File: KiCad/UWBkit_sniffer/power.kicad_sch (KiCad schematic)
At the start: 0 parts

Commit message: Added components to schematic
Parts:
- added C10, C9: 10u, Capacitor_SMD:C_0603_1608Metric, symbol Device:C_Small
- added C8: 100n, Capacitor_SMD:C_0603_1608Metric, symbol Device:C_Small
- added D4: R, LED_SMD:LED_0603_1608Metric, symbol Device:LED_Small
- added L3: 2.2u, Inductor_SMD:L_0805_2012Metric, symbol Device:L_Small
- added R8: 3k3, Resistor_SMD:R_0603_1608Metric, symbol Device:R_Small
- added TP8: TestPoint_Small, TestPoint:TestPoint_Pad_D1.0mm, symbol Connector:TestPoint_Small
- added U4: XC9285B33CMR-G, Package_TO_SOT_SMD:SOT-23-5, symbol DCDC_Converter_Custom:XC9285B33CMR-G
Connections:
- new net: L3.1, U4.5 (Lx)
- new net: D4.1 (K), R8.1
- new net +3V3: C10.1, D4.2 (A), L3.2, TP8.1, U4.4 (VOUT)
- new net +5V: C8.1, C9.1, U4.1 (VIN), U4.3 (EN)
- new net GND: C10.2, C8.2, C9.2, R8.2, U4.2 (GND)
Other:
- note added: "Power LED"
- note added: "Unnecessary when using the USB peripheral directly"

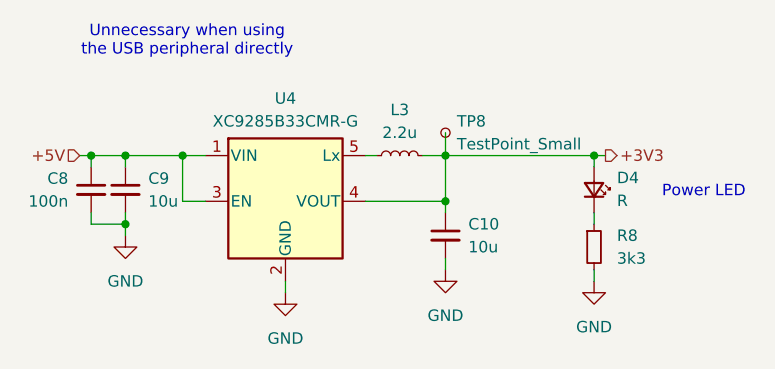
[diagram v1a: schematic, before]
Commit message: United 5V rails, modified layout of connectors
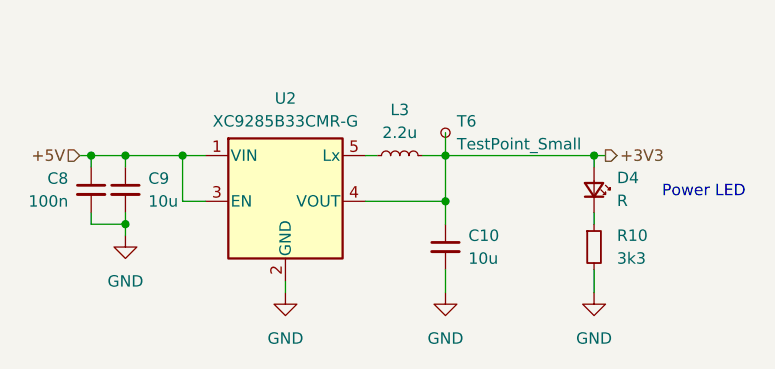
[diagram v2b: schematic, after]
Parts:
- renumbered R8 to R10, TP8 to T6, U4 to U2
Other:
- note removed: "Unnecessary when using the USB peripheral directly"
- moved on the sheet: C10
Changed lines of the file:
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@@
-		)
-	)
-	(text "Unnecessary when using \nthe USB peripheral directly"
-		(exclude_from_sim no)
-		(at 121.158 81.28 0)
-		(effects
-			(font
-				(size 1.27 1.27)
-			)
 		)
 	)
@@
 	(wire
 		(pts
-			(xy 149.86 99.06) (xy 149.86 100.33)
-		)
-		(stroke
-			(width 0)
-			(type default)
-		)
-	)
-	(wire
-		(pts
-			(xy 166.37 106.68) (xy 166.37 107.95)
+			(xy 149.86 99.06) (xy 149.86 101.6)
+		)
+		(stroke
+			(width 0)
+			(type default)
+		)
+	)
+	(wire
+		(pts
+			(xy 166.37 106.68) (xy 166.37 109.22)
 		)
 		(stroke
@@
 	(wire
 		(pts
-			(xy 149.86 105.41) (xy 149.86 106.68)
+			(xy 149.86 106.68) (xy 149.86 109.22)
 		)
 		(stroke
@@
 		(dnp no)
 		(fields_autoplaced yes)
-		(property "Reference" "#PWR034"
+		(property "Reference" "#PWR048"
 			(at 132.08 115.57 0)
 			(effects
@@
 			(project "UWBkit_sniffer"
 				(path "/7666dc1a-7b28-48ea-a5e3-eea89f700cea/10e613d1-a26e-4277-8fad-c08e21526a22"
-					(reference "#PWR034")
+					(reference "#PWR048")
 					(unit 1)
 				)
@@
 	(symbol
 		(lib_id "Device:C_Small")
-		(at 149.86 102.87 0)
+		(at 149.86 104.14 0)
 		(unit 1)
 		(exclude_from_sim no)
@@
 		(dnp no)
 		(property "Reference" "C10"
-			(at 152.4 101.6062 0)
+			(at 152.4 102.8762 0)
 			(effects
 				(font
@@
 		)
 		(property "Value" "10u"
-			(at 152.4 104.1462 0)
+			(at 152.4 105.4162 0)
 			(effects
 				(font
@@
 		)
 		(property "Footprint" "Capacitor_SMD:C_0603_1608Metric"
-			(at 149.86 102.87 0)
+			(at 149.86 104.14 0)
 			(effects
 				(font
@@
 		)
 		(property "Datasheet" "~"
-			(at 149.86 102.87 0)
+			(at 149.86 104.14 0)
 			(effects
 				(font
@@
 		)
 		(property "Description" "Unpolarized capacitor, small symbol"
-			(at 149.86 102.87 0)
+			(at 149.86 104.14 0)
 			(effects
 				(font
@@
 		(on_board yes)
 		(dnp no)
-		(property "Reference" "TP8"
+		(property "Reference" "T6"
 			(at 151.13 90.1699 0)
 			(effects
@@
 			(project "UWBkit_sniffer"
 				(path "/7666dc1a-7b28-48ea-a5e3-eea89f700cea/10e613d1-a26e-4277-8fad-c08e21526a22"
-					(reference "TP8")
+					(reference "T6")
 					(unit 1)
 				)
@@
 	(symbol
 		(lib_id "power:GND")
-		(at 149.86 106.68 0)
+		(at 149.86 109.22 0)
 		(unit 1)
 		(exclude_from_sim no)
@@
 		(dnp no)
 		(fields_autoplaced yes)
-		(property "Reference" "#PWR032"
-			(at 149.86 113.03 0)
+		(property "Reference" "#PWR049"
+			(at 149.86 115.57 0)
 			(effects
 				(font
@@
 		)
 		(property "Value" "GND"
-			(at 149.86 111.76 0)
+			(at 149.86 114.3 0)
 			(effects
 				(font
@@
 		)
 		(property "Footprint" ""
-			(at 149.86 106.68 0)
+			(at 149.86 109.22 0)
 			(effects
 				(font
@@
 		)
 		(property "Datasheet" ""
-			(at 149.86 106.68 0)
+			(at 149.86 109.22 0)
 			(effects
 				(font
@@
 		)
 		(property "Description" "Power symbol creates a global label with name \"GND\" , ground"
-			(at 149.86 106.68 0)
+			(at 149.86 109.22 0)
 			(effects
 				(font
@@
 			(project "UWBkit_sniffer"
 				(path "/7666dc1a-7b28-48ea-a5e3-eea89f700cea/10e613d1-a26e-4277-8fad-c08e21526a22"
-					(reference "#PWR032")
+					(reference "#PWR049")
 					(unit 1)
 				)
@@
 	(symbol
 		(lib_id "power:GND")
-		(at 166.37 107.95 0)
+		(at 166.37 109.22 0)
 		(unit 1)
 		(exclude_from_sim no)
@@
 		(dnp no)
 		(fields_autoplaced yes)
-		(property "Reference" "#PWR033"
+		(property "Reference" "#PWR050"
+			(at 166.37 115.57 0)
+			(effects
+				(font
+					(size 1.27 1.27)
+				)
+				(hide yes)
+			)
+		)
+		(property "Value" "GND"
 			(at 166.37 114.3 0)
 			(effects
@@
 					(size 1.27 1.27)
 				)
-				(hide yes)
-			)
-		)
-		(property "Value" "GND"
-			(at 166.37 113.03 0)
-			(effects
-				(font
-					(size 1.27 1.27)
-				)
 			)
 		)
 		(property "Footprint" ""
-			(at 166.37 107.95 0)
+			(at 166.37 109.22 0)
 			(effects
 				(font
@@
 		)
 		(property "Datasheet" ""
-			(at 166.37 107.95 0)
+			(at 166.37 109.22 0)
 			(effects
 				(font
@@
 		)
 		(property "Description" "Power symbol creates a global label with name \"GND\" , ground"
-			(at 166.37 107.95 0)
+			(at 166.37 109.22 0)
 			(effects
 				(font
@@
 			(project "UWBkit_sniffer"
 				(path "/7666dc1a-7b28-48ea-a5e3-eea89f700cea/10e613d1-a26e-4277-8fad-c08e21526a22"
-					(reference "#PWR033")
+					(reference "#PWR050")
 					(unit 1)
 				)
@@
 		(dnp no)
 		(fields_autoplaced yes)
-		(property "Reference" "U4"
+		(property "Reference" "U2"
 			(at 132.08 87.63 0)
 			(effects
@@
 			(project "UWBkit_sniffer"
 				(path "/7666dc1a-7b28-48ea-a5e3-eea89f700cea/10e613d1-a26e-4277-8fad-c08e21526a22"
-					(reference "U4")
+					(reference "U2")
 					(unit 1)
 				)
@@
 		(dnp no)
 		(fields_autoplaced yes)
-		(property "Reference" "R8"
+		(property "Reference" "R10"
 			(at 168.91 102.8699 0)
 			(effects
@@
 			(project "UWBkit_sniffer"
 				(path "/7666dc1a-7b28-48ea-a5e3-eea89f700cea/10e613d1-a26e-4277-8fad-c08e21526a22"
-					(reference "R8")
+					(reference "R10")
 					(unit 1)
 				)
@@
 		(dnp no)
 		(fields_autoplaced yes)
-		(property "Reference" "#PWR030"
+		(property "Reference" "#PWR047"
 			(at 114.3 109.22 0)
 			(effects
@@
 			(project "UWBkit_sniffer"
 				(path "/7666dc1a-7b28-48ea-a5e3-eea89f700cea/10e613d1-a26e-4277-8fad-c08e21526a22"
-					(reference "#PWR030")
+					(reference "#PWR047")
 					(unit 1)
 				)

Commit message: Removed UWA.01, added CTS/RTS connections
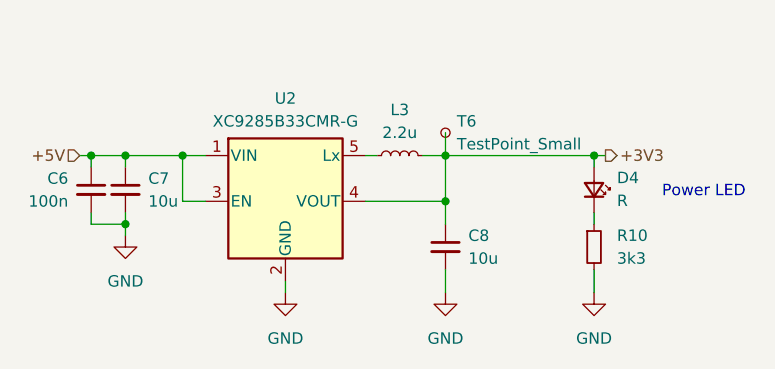
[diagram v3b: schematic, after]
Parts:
- renumbered C8 to C6, C9 to C7, C10 to C8
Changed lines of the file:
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@@
 		(dnp no)
 		(fields_autoplaced yes)
-		(property "Reference" "#PWR048"
+		(property "Reference" "#PWR047"
 			(at 132.08 115.57 0)
 			(effects
@@
 			(project "UWBkit_sniffer"
 				(path "/7666dc1a-7b28-48ea-a5e3-eea89f700cea/10e613d1-a26e-4277-8fad-c08e21526a22"
-					(reference "#PWR048")
+					(reference "#PWR047")
 					(unit 1)
 				)
@@
 		(on_board yes)
 		(dnp no)
-		(property "Reference" "C10"
+		(property "Reference" "C8"
 			(at 152.4 102.8762 0)
 			(effects
@@
 			(project "UWBkit_sniffer"
 				(path "/7666dc1a-7b28-48ea-a5e3-eea89f700cea/10e613d1-a26e-4277-8fad-c08e21526a22"
-					(reference "C10")
+					(reference "C8")
 					(unit 1)
 				)
@@
 		(on_board yes)
 		(dnp no)
-		(property "Reference" "C9"
+		(property "Reference" "C7"
 			(at 116.84 96.5262 0)
 			(effects
@@
 			(project "UWBkit_sniffer"
 				(path "/7666dc1a-7b28-48ea-a5e3-eea89f700cea/10e613d1-a26e-4277-8fad-c08e21526a22"
-					(reference "C9")
+					(reference "C7")
 					(unit 1)
 				)
@@
 		(on_board yes)
 		(dnp no)
-		(property "Reference" "C8"
+		(property "Reference" "C6"
 			(at 107.95 96.5262 0)
 			(effects
@@
 			(project "UWBkit_sniffer"
 				(path "/7666dc1a-7b28-48ea-a5e3-eea89f700cea/10e613d1-a26e-4277-8fad-c08e21526a22"
-					(reference "C8")
+					(reference "C6")
 					(unit 1)
 				)
@@
 		(dnp no)
 		(fields_autoplaced yes)
-		(property "Reference" "#PWR049"
+		(property "Reference" "#PWR048"
 			(at 149.86 115.57 0)
 			(effects
@@
 			(project "UWBkit_sniffer"
 				(path "/7666dc1a-7b28-48ea-a5e3-eea89f700cea/10e613d1-a26e-4277-8fad-c08e21526a22"
-					(reference "#PWR049")
+					(reference "#PWR048")
 					(unit 1)
 				)
@@
 		(dnp no)
 		(fields_autoplaced yes)
-		(property "Reference" "#PWR050"
+		(property "Reference" "#PWR049"
 			(at 166.37 115.57 0)
 			(effects
@@
 			(project "UWBkit_sniffer"
 				(path "/7666dc1a-7b28-48ea-a5e3-eea89f700cea/10e613d1-a26e-4277-8fad-c08e21526a22"
-					(reference "#PWR050")
+					(reference "#PWR049")
 					(unit 1)
 				)
@@
 		(dnp no)
 		(fields_autoplaced yes)
-		(property "Reference" "#PWR047"
+		(property "Reference" "#PWR046"
 			(at 114.3 109.22 0)
 			(effects
@@
 			(project "UWBkit_sniffer"
 				(path "/7666dc1a-7b28-48ea-a5e3-eea89f700cea/10e613d1-a26e-4277-8fad-c08e21526a22"
-					(reference "#PWR047")
-					(unit 1)
-				)
+					(reference "#PWR046")
+					(unit 1)
+				)

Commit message: Improved placement of ICs and ports and the board is now smaller
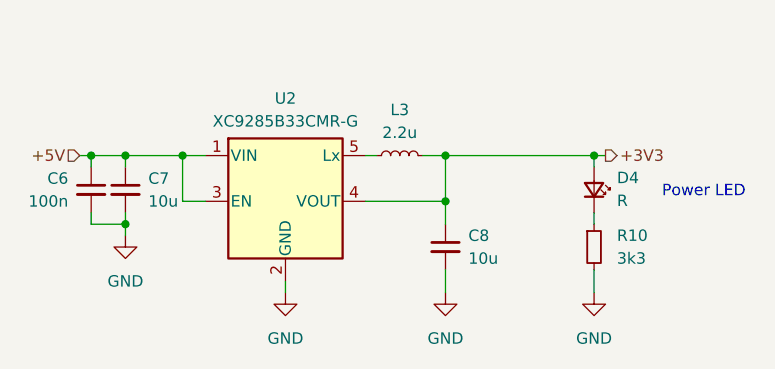
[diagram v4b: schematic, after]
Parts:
- removed T6: TestPoint_Small, TestPoint:TestPoint_Pad_D1.0mm, symbol Connector:TestPoint_Small
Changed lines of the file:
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@@
-	(wire
-		(pts
-			(xy 149.86 91.44) (xy 149.86 93.98)
-		)
-		(stroke
-			(width 0)
-			(type default)
-		)
-	)
 	(wire
 		(pts
@@
 					(unit 1)
 				)
-			)
-		)
-	)
-	(symbol
-		(lib_id "Connector:TestPoint_Small")
-		(at 149.86 91.44 0)
-		(unit 1)
-		(exclude_from_sim no)
-		(in_bom no)
-		(on_board yes)
-		(dnp no)
-		(property "Reference" "T6"
-			(at 151.13 90.1699 0)
-			(effects
-				(font
-					(size 1.27 1.27)
-				)
-				(justify left)
-			)
-		)
-		(property "Value" "TestPoint_Small"
-			(at 151.13 92.7099 0)
-			(effects
-				(font
-					(size 1.27 1.27)
-				)
-				(justify left)
-			)
-		)
-		(property "Footprint" "TestPoint:TestPoint_Pad_D1.0mm"
-			(at 154.94 91.44 0)
-			(effects
-				(font
-					(size 1.27 1.27)
-				)
-				(hide yes)
-			)
-		)
-		(property "Datasheet" "~"
-			(at 154.94 91.44 0)
-			(effects
-				(font
-					(size 1.27 1.27)
-				)
-				(hide yes)
-			)
-		)
-		(property "Description" "test point"
-			(at 149.86 91.44 0)
-			(effects
-				(font
-					(size 1.27 1.27)
-				)
-				(hide yes)
-			)
-		)
-		(pin "1"
-		)
-		(instances
-			(project "UWBkit_sniffer"
-				(path "/7666dc1a-7b28-48ea-a5e3-eea89f700cea/10e613d1-a26e-4277-8fad-c08e21526a22"
-					(reference "T6")
-					(unit 1)
-				)

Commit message: Release V1.0
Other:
- title: (none) -> Power
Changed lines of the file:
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@@
 	(generator_version "9.0")
 	(paper "A4")
+	(title_block
+		(title "Power")
+		(date "2026-02-24")
+		(rev "1.0")
+	)
 	(text "Power LED"
 		(exclude_from_sim no)
